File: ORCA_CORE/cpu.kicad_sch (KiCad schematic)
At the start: 32 parts, among them J10 Raspberry_Pi_2_3, J11 wheel_left, J8 wheel_front, J9 wheel_right, Q1 BSS138, Q2 BSS138, Q8 BSS138, U14 BNO055, U18 TLP293, U19 TLP293, U2 PCA9685PW_Q900_118, U20 TLP293

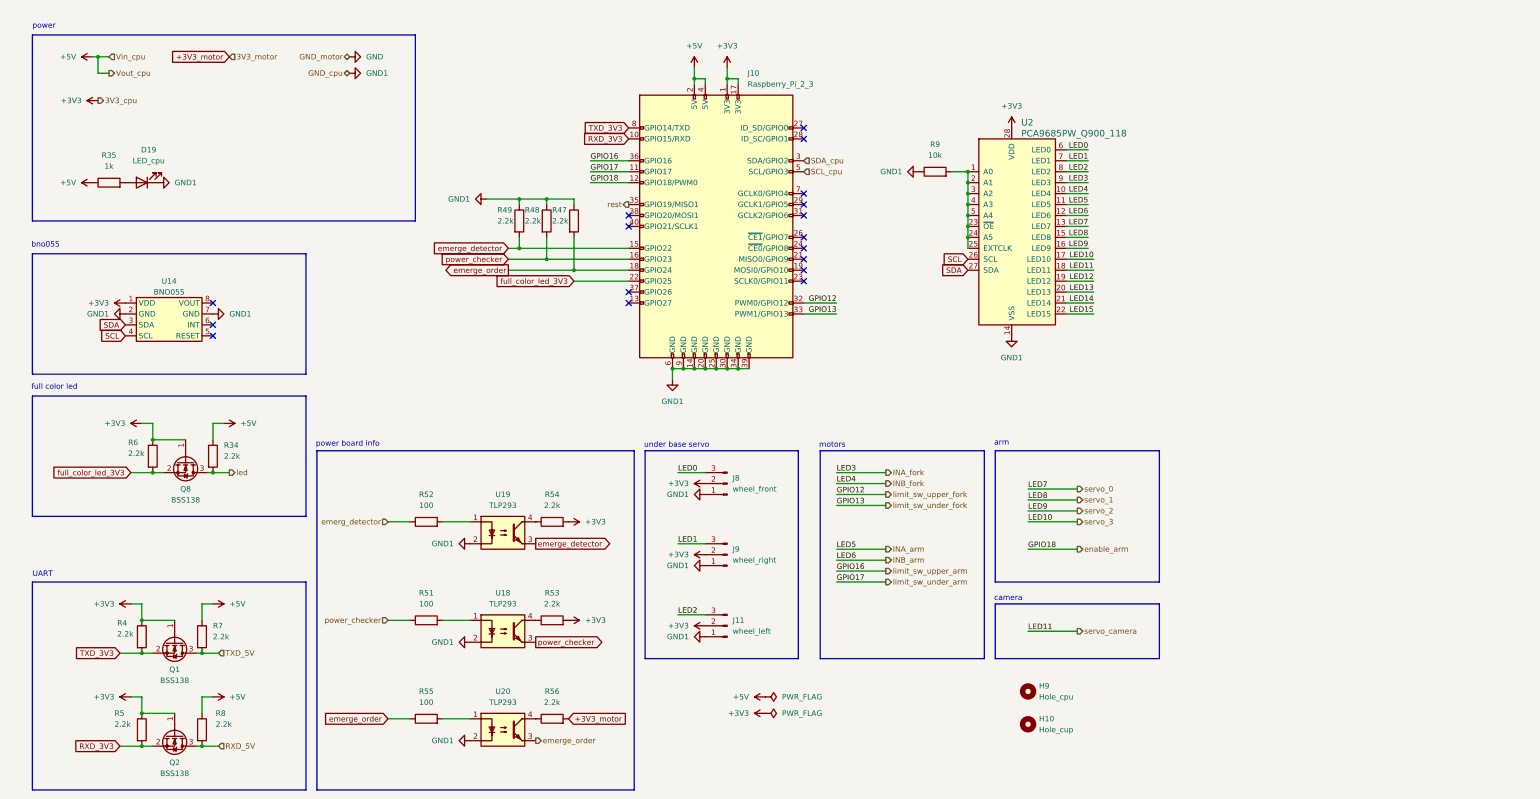
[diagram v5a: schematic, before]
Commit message: complete attaching footprint of CORE
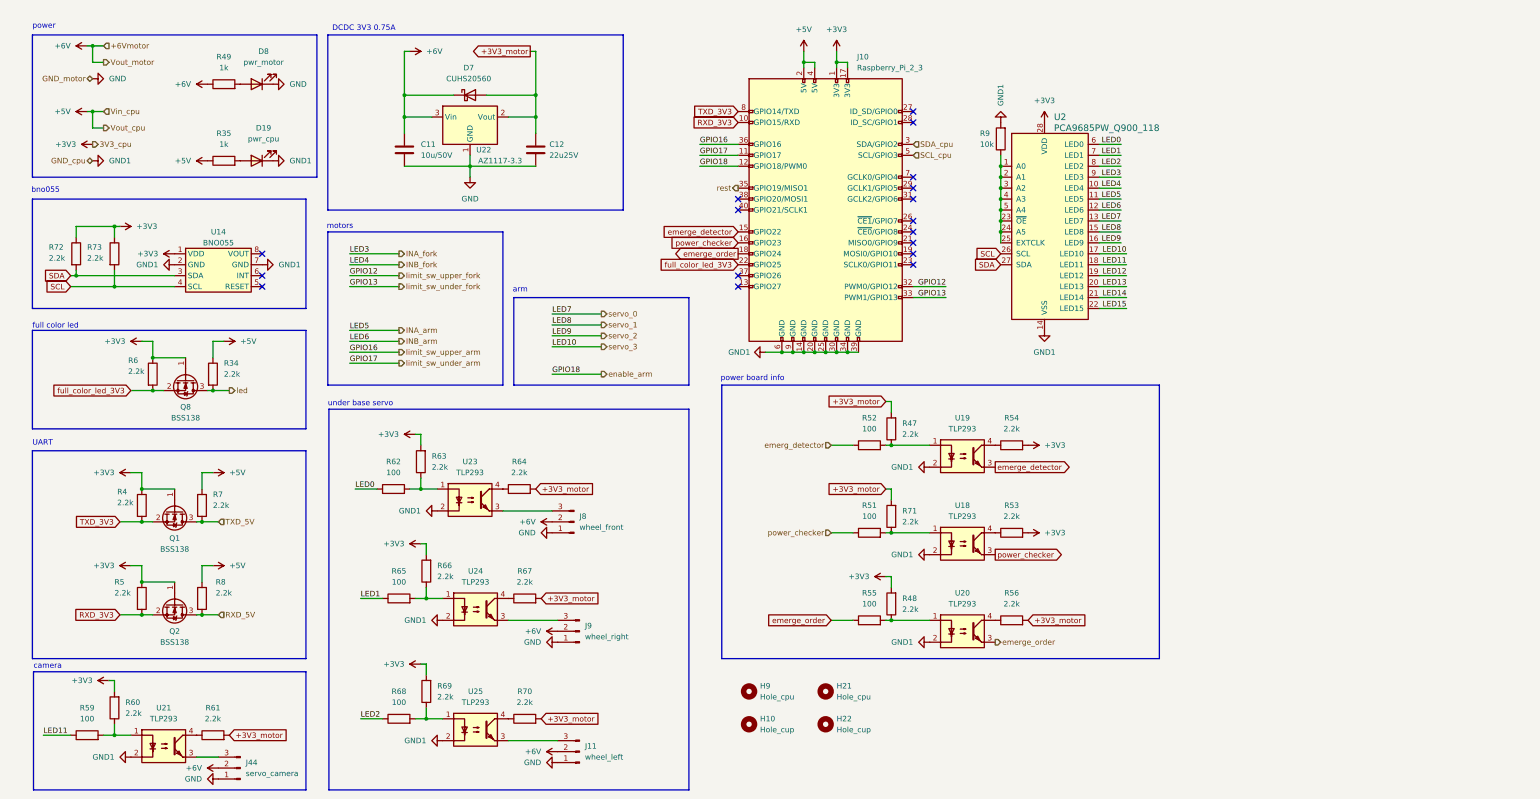
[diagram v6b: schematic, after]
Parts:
- added C11: 10u/50V, Capacitor_SMD:C_1206_3216Metric_Pad1.33x1.80mm_HandSolder, symbol Device:C
- added C12: 22u25V, Capacitor_SMD:C_0805_2012Metric_Pad1.18x1.45mm_HandSolder, symbol Device:C
- added D7: CUHS20560, Diode:Diode_US2H, symbol Device:D_Schottky
- added D8: pwr_motor, LED_SMD:LED_0603_1608Metric_Pad1.05x0.95mm_HandSolder, symbol Device:LED_Filled
- added H21: Hole_cpu, MountingHole:MountingHole_3.2mm_M3, symbol Mechanical:MountingHole
- added H22: Hole_cup, MountingHole:MountingHole_3.2mm_M3, symbol Mechanical:MountingHole
- added J44: servo_camera, Connector_PinHeader_2.54mm:PinHeader_1x03_P2.54mm_Vertical, symbol Connector:Conn_01x03_Pin
- added R59, R62, R65, R68: 100, Resistor_SMD:R_0603_1608Metric_Pad0.98x0.95mm_HandSolder, symbol Device:R
- added R60, R61, R63, R64, R66, R67, R69, R70, R71, R72, R73: 2.2k, Resistor_SMD:R_0603_1608Metric_Pad0.98x0.95mm_HandSolder, symbol Device:R
- added U21, U23, U24, U25: TLP293, Package_SO:SOIC-4_4.55x2.6mm_P1.27mm, symbol Isolator:TLP293
- added U22: AZ1117-3.3, Package_TO_SOT_SMD:SOT-223-3_TabPin2, symbol mylib:AZ1117-3.3V
- D19: value LED_cpu -> pwr_cpu
- J11, J8, J9: footprint (none) -> Connector_PinHeader_2.54mm:PinHeader_1x03_P2.54mm_Vertical
- R49: value 2.2k -> 1k
- R51, R52, R53, R54, R55, R56, R9: footprint (none) -> Resistor_SMD:R_0603_1608Metric_Pad0.98x0.95mm_HandSolder
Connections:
- net +3V3: now also R48.2, R60.2, R63.2, R66.2, R69.2, R72.1, R73.1; no longer J11.2 (Pin_2), J8.2 (Pin_2), J9.2 (Pin_2)
- net +3V3_motor: now also R47.2, C12.1, D7.2 (A), R61.2, R64.2, R67.2, R70.2, R71.2, U22.2 (Vout)
- net GND: now also J11.1 (Pin_1), J8.1 (Pin_1), J9.1 (Pin_1), C11.2, C12.2, D8.1 (K), J44.1 (Pin_1), U22.1 (GND)
- net GND1: now also R9.2, U21.2, U23.2, U24.2, U25.2; no longer J11.1 (Pin_1), J8.1 (Pin_1), J9.1 (Pin_1), R47.1, R48.1, R49.1, R9.1
- net LED0: now also R62.1; no longer J8.3 (Pin_3)
- net LED1: now also R65.1; no longer J9.3 (Pin_3)
- net LED2: now also R68.1; no longer J11.3 (Pin_3)
- net SCL: now also R73.2
- net SDA: now also R72.2
- net emerge_detector: no longer R49.2
- net emerge_order: no longer R47.2
- net power_checker: no longer R48.2
- net at R52.2, U19.1: now also R47.1
- net at R51.2, U18.1: now also R71.1
- net at R55.2, U20.1: now also R48.1
- net at U2.1 (A0), U2.2 (A1), U2.23 (~{OE})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: now also R9.1; no longer R9.2
- net servo_camera renamed LED11
- net LED11: now also R59.1
- new net: R68.2, R69.1, U25.1
- new net: J11.3 (Pin_3), U25.3
- new net: R70.1, U25.4
- new net: J8.3 (Pin_3), U23.3
- new net: R67.1, U24.4
- new net: R61.1, U21.4
- new net: R64.1, U23.4
- new net: R62.2, R63.1, U23.1
- new net: R65.2, R66.1, U24.1
- new net: D8.2 (A), R49.2
- new net: J44.3 (Pin_3), U21.3
- new net: R59.2, R60.1, U21.1
- new net: J9.3 (Pin_3), U24.3
- new net +6V: C11.1, D7.1 (K), J11.2 (Pin_2), J44.2 (Pin_2), J8.2 (Pin_2), J9.2 (Pin_2), R49.1, U22.3 (Vin)
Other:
- note added: "DCDC 3V3 0.75A"
- moved on the sheet: D19, H10, H9, J10, J11, J8, J9, Q1, Q2, Q8, R34, R35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

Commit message: made board outline and import it
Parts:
- J8: footprint Connector_PinHeader_2.54mm:PinHeader_1x03_P2.54mm_Vertical -> Connector_PinHeader_2.54mm:PinHeader_1x03_P2.54mm_Horizontal
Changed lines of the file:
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@@
 			)
 		)
-		(property "Footprint" "Connector_PinHeader_2.54mm:PinHeader_1x03_P2.54mm_Vertical"
+		(property "Footprint" "Connector_PinHeader_2.54mm:PinHeader_1x03_P2.54mm_Horizontal"
 			(at 143.51 130.81 0)
 			(effects
@@
 			)
 		)
+		(pin "3"
+		)
+		(pin "1"
+		)
 		(pin "2"
 		)
-		(pin "3"
-		)
-		(pin "1"
-		)
-		(instances
-			(project "ORCA_CORE"
+		(instances
+			(project ""
 				(path "/895d6bb7-4008-488b-a34b-0077e9f7e4a1/e25f2ef8-8e13-4e8d-9b3a-975318177c66"
 					(reference "J11")

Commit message: place most of footprints. test replicate
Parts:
- J10: footprint cpu:raspberrypi_Zero_W_Vertical -> cpu:raspberrypi_Zerp_W_horisontal
- J44, J9: footprint Connector_PinHeader_2.54mm:PinHeader_1x03_P2.54mm_Vertical -> Connector_PinHeader_2.54mm:PinHeader_1x03_P2.54mm_Horizontal
- U14: footprint IMU:BNO055 -> IMU:BNO055_short
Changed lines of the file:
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@@
 			)
 		)
-		(property "Footprint" "cpu:raspberrypi_Zero_W_Vertical"
+		(property "Footprint" "cpu:raspberrypi_Zerp_W_horisontal"
 			(at 201.93 58.42 0)
 			(effects
@@
 			)
 		)
-		(property "Footprint" "Connector_PinHeader_2.54mm:PinHeader_1x03_P2.54mm_Vertical"
+		(property "Footprint" "Connector_PinHeader_2.54mm:PinHeader_1x03_P2.54mm_Horizontal"
 			(at 66.04 187.96 0)
 			(effects
@@
 			)
 		)
-		(property "Footprint" "IMU:BNO055"
+		(property "Footprint" "IMU:BNO055_short"
 			(at 60.96 72.39 0)
 			(effects
@@
 			)
 		)
-		(property "Footprint" "Connector_PinHeader_2.54mm:PinHeader_1x03_P2.54mm_Vertical"
+		(property "Footprint" "Connector_PinHeader_2.54mm:PinHeader_1x03_P2.54mm_Horizontal"
 			(at 144.78 156.21 0)
 			(effects
